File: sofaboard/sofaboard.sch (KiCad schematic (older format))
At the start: 180 parts, among them J1 USB_B_Micro, J2 USB4085-GF-A_REVA, SW1 SW_Push, SW10 SW_Push, SW11 SW_Push, SW12 SW_Push, SW13 SW_Push, SW14 SW_Push, SW15 SW_Push, SW16 SW_Push, SW17 SW_Push, SW18 SW_Push, SW19 SW_Push, SW2 SW_Push, SW20 SW_Push, SW21 SW_Push, SW22 SW_Push, SW23 SW_Push, SW24 SW_Push, SW25 SW_Push, SW26 SW_Push, SW27 SW_Push, SW28 SW_Push, SW29 SW_Push, SW3 SW_Push, SW30 SW_Push, SW31 SW_Push, SW32 SW_Push, SW33 SW_Push, SW34 SW_Push, SW35 SW_Push, SW36 SW_Push, SW37 SW_Push, SW38 SW_Push, SW39 SW_Push, SW4 SW_Push, SW40 SW_Push, SW41 SW_Push, SW42 SW_Push, SW43 SW_Push, SW44 SW_Push, SW45 SW_Push, SW46 SW_Push, SW47 SW_Push, SW48 SW_Push, SW49 SW_Push, SW5 SW_Push, SW50 SW_Push, SW51 SW_Push, SW52 SW_Push, SW53 SW_Push, SW54 SW_Push, SW55 SW_Push, SW56 SW_Push, SW57 SW_Push, SW58 SW_Push, SW59 SW_Push, SW6 SW_Push, SW60 SW_Push, SW61 SW_Push, SW62 SW_Push, SW63 SW_Push, SW64 SW_Push, SW65 SW_Push, SW66 SW_Push, SW67 SW_Push, SW68 SW_Push, SW69 SW_Push, SW7 SW_Push, SW70 SW_Push, SW71 SW_Push, SW72 SW_Push, SW73 SW_Push, SW74 SW_Push, SW75 SW_Push, SW76 SW_Push, SW77 SW_Push, SW78 SW_Push, SW79 SW_Push, SW8 SW_Push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

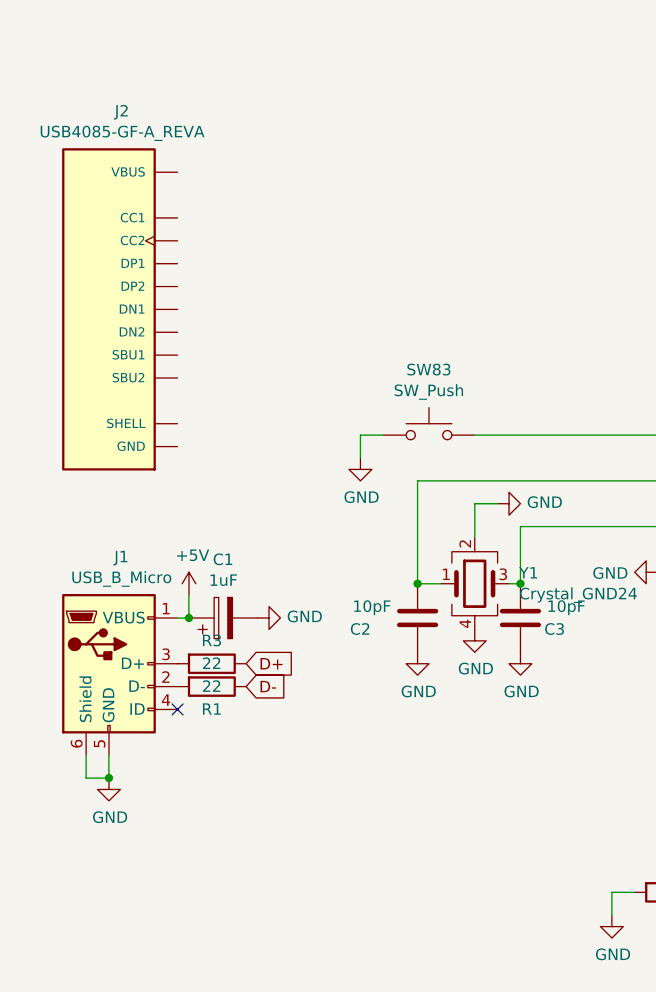
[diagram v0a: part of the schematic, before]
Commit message: reconnect diodes
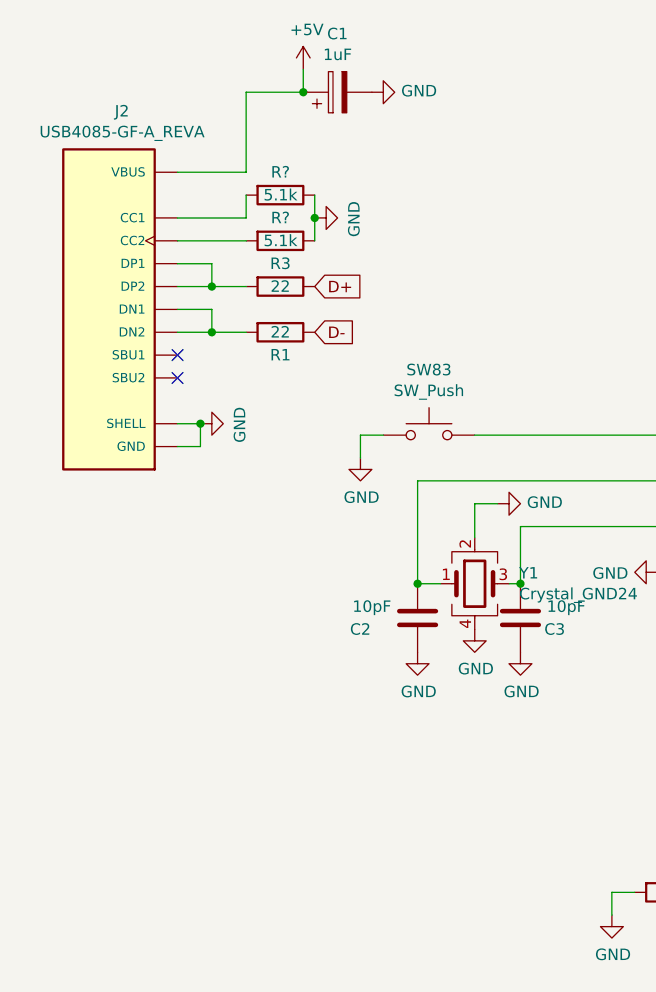
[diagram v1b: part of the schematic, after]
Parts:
- removed J1: USB_B_Micro, Connector_USB:USB_Micro-B_Amphenol_10103594-0001LF_Horizontal, symbol sofaboard-rescue:USB_B_Micro-Connector
- added R? (x2): 5.1k, Resistor_SMD:R_0805_2012Metric_Pad1.15x1.40mm_HandSolder, symbol Device:R
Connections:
- net +5V: now also J2.A4 (VBUS), J2.A9 (VBUS), J2.B4 (VBUS), J2.B9 (VBUS)
- net GND: now also J2.A1 (GND), J2.A12 (GND), J2.B1 (GND), J2.B12 (GND), J2.P1 (SHELL), J2.P2 (SHELL), J2.P3 (SHELL), J2.P4 (SHELL), R?.1, R?.1
- net at R1.2: now also J2.A7 (DN1), J2.B7 (DN2)
- net at R3.2: now also J2.A6 (DP1), J2.B6 (DP2)
- net at J2.A5 (CC1): now also R?.2
- net at J2.B5 (CC2): now also R?.2
- no-connect marks 27 -> 28
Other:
- moved on the sheet: C1, R1, R3
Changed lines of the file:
@@
-$EndComp
-$Comp
-L sofaboard-rescue:USB_B_Micro-Connector J1
-U 1 1 5CD0EFEC
-P 1750 3900
-F 0 "J1" H 1805 4367 50  0000 C CNN
-F 1 "USB_B_Micro" H 1805 4276 50  0000 C CNN
-F 2 "Connector_USB:USB_Micro-B_Amphenol_10103594-0001LF_Horizontal" H 1900 3850 50  0001 C CNN
-F 3 "~" H 1900 3850 50  0001 C CNN
-	1    1750 3900
-	1    0    0    -1
 $EndComp
 $Comp
 L power:+5V #PWR0101
 U 1 1 5CD12DE2
-P 2100 3600
-F 0 "#PWR0101" H 2100 3450 50  0001 C CNN
-F 1 "+5V" H 2115 3773 50  0000 C CNN
-F 2 "" H 2100 3600 50  0001 C CNN
-F 3 "" H 2100 3600 50  0001 C CNN
-	1    2100 3600
-	1    0    0    -1
-$EndComp
-Wire Wire Line
-	2050 3700 2100 3700
-Wire Wire Line
-	2100 3700 2100 3600
+P 2600 1300
+F 0 "#PWR0101" H 2600 1150 50  0001 C CNN
+F 1 "+5V" H 2615 1473 50  0000 C CNN
+F 2 "" H 2600 1300 50  0001 C CNN
+F 3 "" H 2600 1300 50  0001 C CNN
+	1    2600 1300
+	1    0    0    -1
+$EndComp
+Wire Wire Line
+	2600 1400 2600 1300
 $Comp
 L power:+5V #PWR0102
@@
 L Device:R R3
 U 1 1 5CE1B4FE
-P 2200 3900
-F 0 "R3" V 2100 3900 50  0000 C CNN
-F 1 "22" V 2200 3900 50  0000 C CNN
-F 2 "Resistor_SMD:R_0805_2012Metric_Pad1.15x1.40mm_HandSolder" V 2130 3900 50  0001 C CNN
-F 3 "~" H 2200 3900 50  0001 C CNN
-	1    2200 3900
+P 2500 2250
+F 0 "R3" V 2400 2250 50  0000 C CNN
+F 1 "22" V 2500 2250 50  0000 C CNN
+F 2 "Resistor_SMD:R_0805_2012Metric_Pad1.15x1.40mm_HandSolder" V 2430 2250 50  0001 C CNN
+F 3 "~" H 2500 2250 50  0001 C CNN
+	1    2500 2250
 	0    1    1    0
 $EndComp
@@
 L Device:R R1
 U 1 1 5CE1D9C5
-P 2200 4000
-F 0 "R1" V 2300 4000 50  0000 C CNN
-F 1 "22" V 2200 4000 50  0000 C CNN
-F 2 "Resistor_SMD:R_0805_2012Metric_Pad1.15x1.40mm_HandSolder" V 2130 4000 50  0001 C CNN
-F 3 "~" H 2200 4000 50  0001 C CNN
-	1    2200 4000
+P 2500 2450
+F 0 "R1" V 2600 2450 50  0000 C CNN
+F 1 "22" V 2500 2450 50  0000 C CNN
+F 2 "Resistor_SMD:R_0805_2012Metric_Pad1.15x1.40mm_HandSolder" V 2430 2450 50  0001 C CNN
+F 3 "~" H 2500 2450 50  0001 C CNN
+	1    2500 2450
 	0    1    1    0
 $EndComp
@@
 L power:GND #PWR0105
 U 1 1 5CEE2878
-P 1750 4400
-F 0 "#PWR0105" H 1750 4150 50  0001 C CNN
-F 1 "GND" H 1755 4227 50  0000 C CNN
-F 2 "" H 1750 4400 50  0001 C CNN
-F 3 "" H 1750 4400 50  0001 C CNN
-	1    1750 4400
-	1    0    0    -1
-$EndComp
-Wire Wire Line
-	1650 4300 1650 4400
-Wire Wire Line
-	1650 4400 1750 4400
-Wire Wire Line
-	1750 4300 1750 4400
-Connection ~ 1750 4400
+P 2150 2850
+F 0 "#PWR0105" H 2150 2600 50  0001 C CNN
+F 1 "GND" H 2155 2677 50  0000 C CNN
+F 2 "" H 2150 2850 50  0001 C CNN
+F 3 "" H 2150 2850 50  0001 C CNN
+	1    2150 2850
+	0    -1   1    0
+$EndComp
+Wire Wire Line
+	2050 2950 2150 2950
+Wire Wire Line
+	2150 2950 2150 2850
+Wire Wire Line
+	2050 2850 2150 2850
+Connection ~ 2150 2850
 $Comp
 L power:GND #PWR0106
@@
 L Device:CP C1
 U 1 1 5DAF5A2B
-P 2250 3700
-F 0 "C1" V 2505 3700 50  0000 C CNN
-F 1 "1uF" V 2414 3700 50  0000 C CNN
-F 2 "Capacitor_SMD:C_0805_2012Metric_Pad1.15x1.40mm_HandSolder" H 2288 3550 50  0001 C CNN
-F 3 "~" H 2250 3700 50  0001 C CNN
-	1    2250 3700
+P 2750 1400
+F 0 "C1" V 3005 1400 50  0000 C CNN
+F 1 "1uF" V 2914 1400 50  0000 C CNN
+F 2 "Capacitor_SMD:C_0805_2012Metric_Pad1.15x1.40mm_HandSolder" H 2788 1250 50  0001 C CNN
+F 3 "~" H 2750 1400 50  0001 C CNN
+	1    2750 1400
 	0    -1   -1   0
 $EndComp
-Connection ~ 2100 3700
+Connection ~ 2600 1400
 $Comp
 L power:GND #PWR0112
 U 1 1 5DAF5F3F
-P 2400 3700
-F 0 "#PWR0112" H 2400 3450 50  0001 C CNN
-F 1 "GND" V 2405 3572 50  0000 R CNN
-F 2 "" H 2400 3700 50  0001 C CNN
-F 3 "" H 2400 3700 50  0001 C CNN
-	1    2400 3700
+P 2900 1400
+F 0 "#PWR0112" H 2900 1150 50  0001 C CNN
+F 1 "GND" V 2905 1272 50  0000 R CNN
+F 2 "" H 2900 1400 50  0001 C CNN
+F 3 "" H 2900 1400 50  0001 C CNN
+	1    2900 1400
 	0    -1   -1   0
 $EndComp
@@
 	5400 6600 5400 6700
 Connection ~ 5400 6600
-NoConn ~ 2050 4100
 Connection ~ 3100 3550
 Wire Wire Line
@@
 Text GLabel 4700 3900 0    50   Input ~ 0
 D+
-Text GLabel 2350 3900 2    50   Input ~ 0
+Text GLabel 2650 2250 2    50   Input ~ 0
 D+
 Text GLabel 4350 4000 0    50   Input ~ 0
 D-
-Text GLabel 2350 4000 2    50   Input ~ 0
+Text GLabel 2650 2450 2    50   Input ~ 0
 D-
 $Comp
@@
 	-1   0    0    -1
 $EndComp
+Wire Wire Line
+	2350 1400 2600 1400
+Wire Wire Line
+	2200 2150 2200 2250
+Wire Wire Line
+	2200 2250 2050 2250
+Wire Wire Line
+	2050 2150 2200 2150
+Wire Wire Line
+	2350 2250 2200 2250
+Wire Wire Line
+	2050 2350 2200 2350
+Wire Wire Line
+	2200 2350 2200 2450
+Wire Wire Line
+	2200 2450 2050 2450
+Wire Wire Line
+	2200 2450 2350 2450
+NoConn ~ 2050 2650
+NoConn ~ 2050 2550
+Wire Wire Line
+	2050 1750 2350 1750
+Wire Wire Line
+	2350 1750 2350 1400
+Connection ~ 2200 2250
+Connection ~ 2200 2450
+$Comp
+L Device:R R?
+U 1 1 61085BE6
+P 2500 2050
+F 0 "R?" V 2400 2050 50  0000 C CNN
+F 1 "5.1k" V 2500 2050 50  0000 C CNN
+F 2 "Resistor_SMD:R_0805_2012Metric_Pad1.15x1.40mm_HandSolder" V 2430 2050 50  0001 C CNN
+F 3 "~" H 2500 2050 50  0001 C CNN
+	1    2500 2050
+	0    1    1    0
+$EndComp
+$Comp
+L Device:R R?
+U 1 1 61086380
+P 2500 1850
+F 0 "R?" V 2400 1850 50  0000 C CNN
+F 1 "5.1k" V 2500 1850 50  0000 C CNN
+F 2 "Resistor_SMD:R_0805_2012Metric_Pad1.15x1.40mm_HandSolder" V 2430 1850 50  0001 C CNN
+F 3 "~" H 2500 1850 50  0001 C CNN
+	1    2500 1850
+	0    1    1    0
+$EndComp
+Wire Wire Line
+	2050 2050 2350 2050
+Wire Wire Line
+	2050 1950 2350 1950
+Wire Wire Line
+	2350 1950 2350 1850
+Wire Wire Line
+	2650 1850 2650 1950
+$Comp
+L power:GND #PWR?
+U 1 1 61110CB6
+P 2650 1950
+F 0 "#PWR?" H 2650 1700 50  0001 C CNN
+F 1 "GND" H 2655 1777 50  0000 C CNN
+F 2 "" H 2650 1950 50  0001 C CNN
+F 3 "" H 2650 1950 50  0001 C CNN
+	1    2650 1950
+	0    -1   1    0
+$EndComp
+Connection ~ 2650 1950
+Wire Wire Line
+	2650 1950 2650 2050
 $EndSCHEMATC

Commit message: refit for order w/einball
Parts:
- added R6: 10k, Resistor_SMD:R_0805_2012Metric, symbol Device:R
- R4, R5: renamed from R?; footprint Resistor_SMD:R_0805_2012Metric_Pad1.15x1.40mm_HandSolder -> Resistor_SMD:R_0805_2012Metric
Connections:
- net +5V: now also R6.1
- net at SW83.2, U1.20 (~RESET): now also R6.2
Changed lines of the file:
@@
 Connection ~ 3100 3550
 Wire Wire Line
-	3350 2900 4800 2900
+	3350 2900 4250 2900
 NoConn ~ 6000 6200
 NoConn ~ 6000 5400
@@
 Connection ~ 2200 2450
 $Comp
-L Device:R R?
+L Device:R R5
 U 1 1 61085BE6
 P 2500 2050
-F 0 "R?" V 2400 2050 50  0000 C CNN
+F 0 "R5" V 2400 2050 50  0000 C CNN
 F 1 "5.1k" V 2500 2050 50  0000 C CNN
-F 2 "Resistor_SMD:R_0805_2012Metric_Pad1.15x1.40mm_HandSolder" V 2430 2050 50  0001 C CNN
+F 2 "Resistor_SMD:R_0805_2012Metric" V 2430 2050 50  0001 C CNN
 F 3 "~" H 2500 2050 50  0001 C CNN
 	1    2500 2050
@@
 $EndComp
 $Comp
-L Device:R R?
+L Device:R R4
 U 1 1 61086380
 P 2500 1850
-F 0 "R?" V 2400 1850 50  0000 C CNN
+F 0 "R4" V 2400 1850 50  0000 C CNN
 F 1 "5.1k" V 2500 1850 50  0000 C CNN
-F 2 "Resistor_SMD:R_0805_2012Metric_Pad1.15x1.40mm_HandSolder" V 2430 1850 50  0001 C CNN
+F 2 "Resistor_SMD:R_0805_2012Metric" V 2430 1850 50  0001 C CNN
 F 3 "~" H 2500 1850 50  0001 C CNN
 	1    2500 1850
@@
 	2650 1850 2650 1950
 $Comp
-L power:GND #PWR?
+L power:GND #PWR01
 U 1 1 61110CB6
 P 2650 1950
-F 0 "#PWR?" H 2650 1700 50  0001 C CNN
+F 0 "#PWR01" H 2650 1700 50  0001 C CNN
 F 1 "GND" H 2655 1777 50  0000 C CNN
 F 2 "" H 2650 1950 50  0001 C CNN
@@
 Wire Wire Line
 	2650 1950 2650 2050
+$Comp
+L Device:R R6
+U 1 1 62942576
+P 4550 2500
+F 0 "R6" V 4650 2500 50  0000 C CNN
+F 1 "10k" V 4550 2500 50  0000 C CNN
+F 2 "Resistor_SMD:R_0805_2012Metric" V 4480 2500 50  0001 C CNN
+F 3 "~" H 4550 2500 50  0001 C CNN
+	1    4550 2500
+	0    1    1    0
+$EndComp
+Wire Wire Line
+	4700 2500 5300 2500
+Connection ~ 5300 2500
+Wire Wire Line
+	4400 2500 4250 2500
+Wire Wire Line
+	4250 2500 4250 2900
+Connection ~ 4250 2900
+Wire Wire Line
+	4250 2900 4800 2900
 $EndSCHEMATC

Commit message: did more things for final order
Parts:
- R1, R3: footprint Resistor_SMD:R_0805_2012Metric_Pad1.15x1.40mm_HandSolder -> Resistor_SMD:R_0805_2012Metric
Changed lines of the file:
@@
 F 0 "R3" V 2400 2250 50  0000 C CNN
 F 1 "22" V 2500 2250 50  0000 C CNN
-F 2 "Resistor_SMD:R_0805_2012Metric_Pad1.15x1.40mm_HandSolder" V 2430 2250 50  0001 C CNN
+F 2 "Resistor_SMD:R_0805_2012Metric" V 2430 2250 50  0001 C CNN
 F 3 "~" H 2500 2250 50  0001 C CNN
 	1    2500 2250
@@
 F 0 "R1" V 2600 2450 50  0000 C CNN
 F 1 "22" V 2500 2450 50  0000 C CNN
-F 2 "Resistor_SMD:R_0805_2012Metric_Pad1.15x1.40mm_HandSolder" V 2430 2450 50  0001 C CNN
+F 2 "Resistor_SMD:R_0805_2012Metric" V 2430 2450 50  0001 C CNN
 F 3 "~" H 2500 2450 50  0001 C CNN
 	1    2500 2450
